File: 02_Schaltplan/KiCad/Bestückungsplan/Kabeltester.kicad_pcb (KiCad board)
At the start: 4 copper layers, 99.7 x 99.7 mm, 253 parts, among them J1 INPUT/MALE-DB9, J10 Conn_02x01, J11 Conn_02x01, J12 Conn_02x01, J13 Conn_02x01, J14 GND, J15 GND, J16 GND, J2 OUTPUT/FEMALE-DB9, J3 SPEED (20k-POTI), J4 VCC, J5 9V_Batt, J6 MEASURE-CON, J7 MEASURE-CON, J8 MEASURE-CON, J9 MEASURE-CON, Q1 SI2318, Q10 Si2301, Q11 BC858, Q2 Si2301, Q3 BSS123, Q4 Si2301, Q5 BSS123, Q6 Si2301, Q7 BSS123, Q8 Si2301, Q9 BSS123, SW1 START, SW2 MODE, SW3 PWR ON/OFF, U1 74HC08PW, U10 74AHC2G08, U11 NE555, U12 74AHC1G32, U13 74LVC1G175, U14 LTC6993, U15 74LVC1G175, U16 74LVC2G14, U17 LMV321AUIDBVR, U18 LMV358MM, U19 INA826AIDRGT, U2 74HC02PW, U20 74HC595, U21 74HC595, U22 74AHC2G08, U23 74HC08PW, U28 74HC1G126, U29 74HC86PW, U3 74AHC1G32, U30 74HC02PW, U31 74HC02PW, U32 74AHC1G14, U34 74HC08PW, U38 DG2535, U39 DG2535, U4 74HC08PW, U5 CD74HC4514M96, U6 SN74LS93, U7 TPS_54331, U8 74AHC1G14

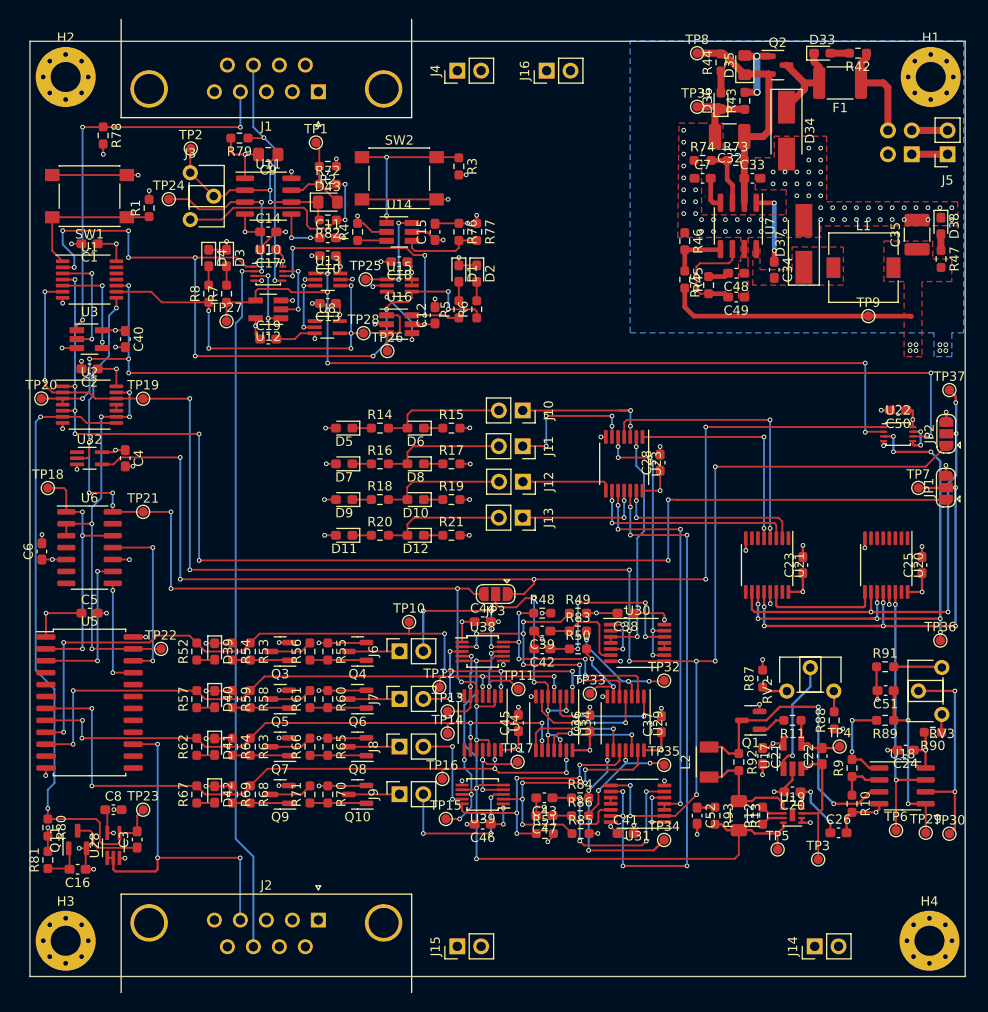
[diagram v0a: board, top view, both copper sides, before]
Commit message: Changes & ADD
+Bestückungsplan
+Auftragsplannung
@ Klärung verschiedener Begrifflichkeiten
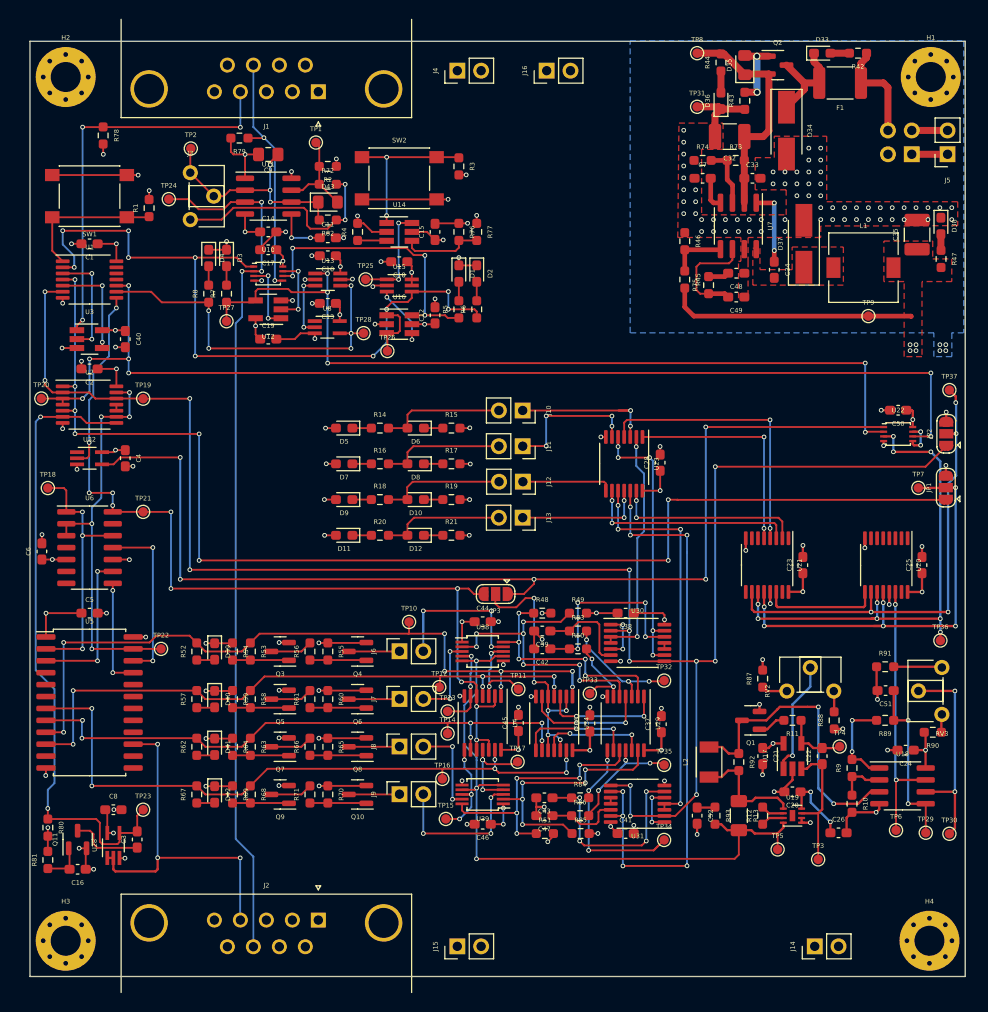
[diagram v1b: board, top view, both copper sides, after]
